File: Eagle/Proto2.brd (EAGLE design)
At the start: 100 x 80 mm, 297 parts, among them Q1 310mA/60V/1.6Ω, Q10 310mA/60V/1.6Ω, Q129 310mA/60V/1.6Ω, Q13 310mA/60V/1.6Ω, Q130 310mA/60V/1.6Ω, Q131 310mA/60V/1.6Ω, Q132 310mA/60V/1.6Ω, Q133 310mA/60V/1.6Ω, Q134 310mA/60V/1.6Ω, Q135 310mA/60V/1.6Ω, Q136 310mA/60V/1.6Ω, Q137 310mA/60V/1.6Ω, Q138 310mA/60V/1.6Ω, Q139 310mA/60V/1.6Ω, Q14 310mA/60V/1.6Ω, Q140 310mA/60V/1.6Ω, Q141 310mA/60V/1.6Ω, Q142 310mA/60V/1.6Ω, Q143 310mA/60V/1.6Ω, Q144 310mA/60V/1.6Ω, Q145 310mA/60V/1.6Ω, Q146 310mA/60V/1.6Ω, Q147 310mA/60V/1.6Ω, Q148 310mA/60V/1.6Ω, Q149 310mA/60V/1.6Ω, Q150 310mA/60V/1.6Ω, Q151 310mA/60V/1.6Ω, Q152 310mA/60V/1.6Ω, Q153 310mA/60V/1.6Ω, Q154 310mA/60V/1.6Ω, Q155 310mA/60V/1.6Ω, Q156 310mA/60V/1.6Ω, Q157 310mA/60V/1.6Ω, Q158 310mA/60V/1.6Ω, Q159 310mA/60V/1.6Ω, Q160 310mA/60V/1.6Ω, Q17 310mA/60V/1.6Ω, Q18 310mA/60V/1.6Ω, Q193 310mA/60V/1.6Ω, Q194 310mA/60V/1.6Ω, Q195 310mA/60V/1.6Ω, Q196 310mA/60V/1.6Ω, Q197 310mA/60V/1.6Ω, Q198 310mA/60V/1.6Ω, Q199 310mA/60V/1.6Ω, Q2 310mA/60V/1.6Ω, Q200 310mA/60V/1.6Ω, Q201 310mA/60V/1.6Ω, Q202 310mA/60V/1.6Ω, Q203 310mA/60V/1.6Ω, Q204 310mA/60V/1.6Ω, Q205 310mA/60V/1.6Ω, Q206 310mA/60V/1.6Ω, Q207 310mA/60V/1.6Ω, Q208 310mA/60V/1.6Ω, Q209 310mA/60V/1.6Ω, Q21 310mA/60V/1.6Ω, Q210 310mA/60V/1.6Ω, Q211 310mA/60V/1.6Ω, Q212 310mA/60V/1.6Ω, Q213 310mA/60V/1.6Ω, Q214 310mA/60V/1.6Ω, Q215 310mA/60V/1.6Ω, Q216 310mA/60V/1.6Ω, Q217 310mA/60V/1.6Ω, Q218 310mA/60V/1.6Ω, Q219 310mA/60V/1.6Ω, Q22 310mA/60V/1.6Ω, Q220 310mA/60V/1.6Ω, Q221 310mA/60V/1.6Ω, Q222 310mA/60V/1.6Ω, Q223 310mA/60V/1.6Ω, Q224 310mA/60V/1.6Ω, Q25 310mA/60V/1.6Ω, Q257 310mA/60V/1.6Ω, Q258 310mA/60V/1.6Ω, Q259 310mA/60V/1.6Ω, Q26 310mA/60V/1.6Ω, Q260 310mA/60V/1.6Ω, Q261 310mA/60V/1.6Ω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

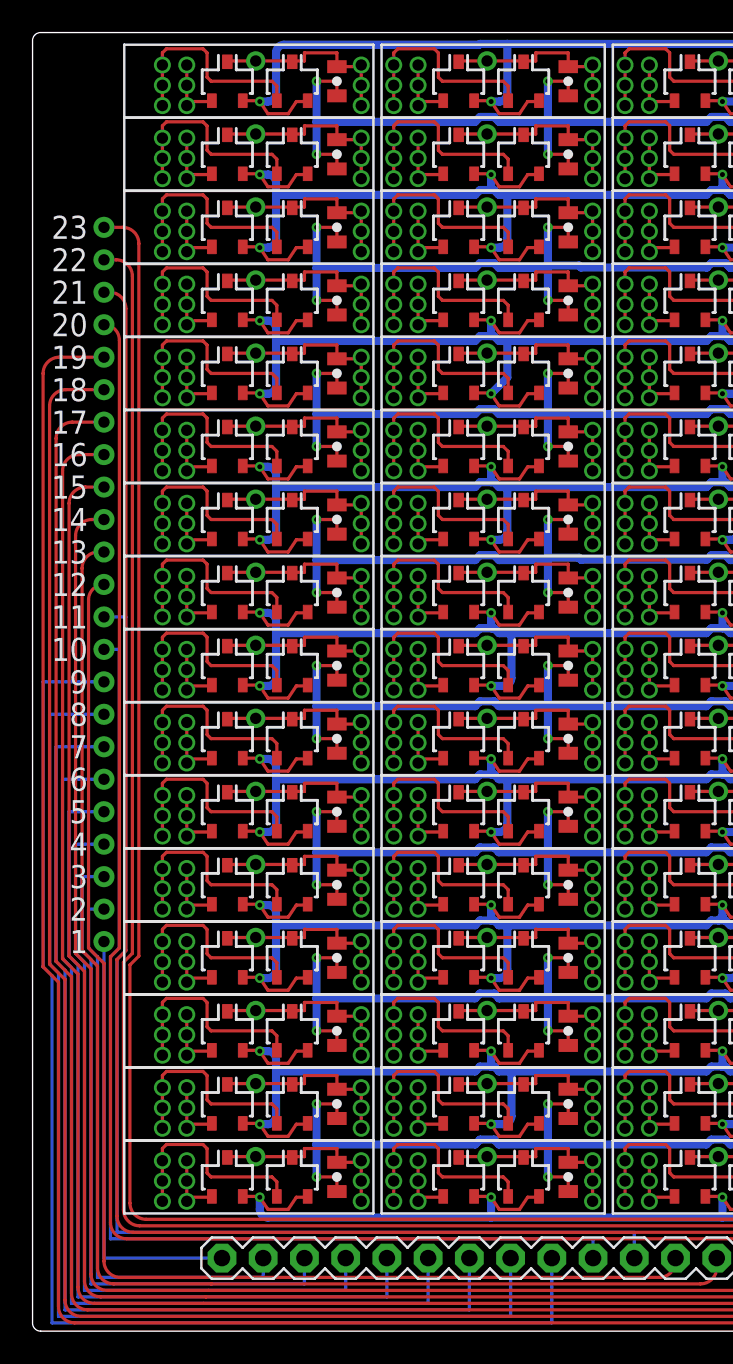
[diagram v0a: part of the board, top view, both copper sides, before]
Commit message: Silk cleanup. Routing of GND instead of floodfill
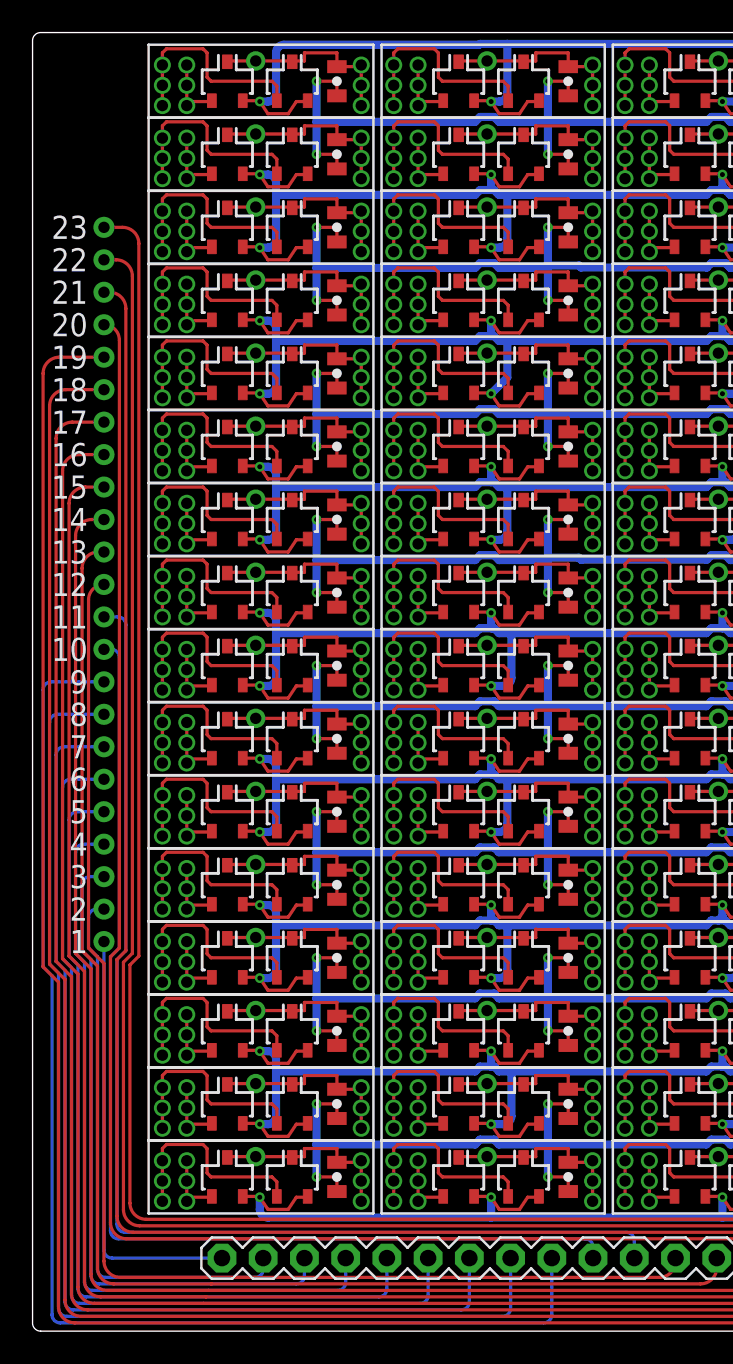
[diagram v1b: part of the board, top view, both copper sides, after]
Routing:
- net P5: track 53.7 -> 52.8 mm
- net P4: track 47.5 -> 46.7 mm
- net P9: track 78.2 -> 77.4 mm
- net P8: track 72.1 -> 71.2 mm
- net P7: track 66.0 -> 65.1 mm
- net P3: track 41.4 -> 40.5 mm
- net P2: track 35.3 -> 34.4 mm
- net P11: track 72.9 -> 72.1 mm
- net P10: track 68.4 -> 67.5 mm
- net P6: track 59.8 -> 59.0 mm
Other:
- board text added: "Dual NOR proto Rev 1"
- board text added: "SmallRoomLabs"

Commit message: Updated boards with pcb template
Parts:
- moved C10 7.00 mm to (93.8, 55.0)
- moved C12 7.00 mm to (93.8, 64.0)
- moved C14 7.00 mm to (93.8, 73.0)
- moved C16 7.00 mm to (93.8, 82.0)
- moved C4 7.00 mm to (93.8, 28.0)
- moved C6 7.00 mm to (93.8, 37.0)
- moved C8 7.00 mm to (93.8, 46.0)
- moved Q1 7.00 mm to (12.0, 16.5)
- moved Q10 7.00 mm to (16.0, 25.5)
- moved Q129 7.00 mm to (40.5, 16.5)
- moved Q13 7.00 mm to (12.0, 30.0)
- moved Q130 7.00 mm to (44.5, 16.5)
- moved Q131 7.00 mm to (40.5, 21.0)
- moved Q132 7.00 mm to (44.5, 21.0)
- moved Q133 7.00 mm to (40.5, 25.5)
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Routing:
- net GND: track 1536.7 -> 1695.6 mm
- net N$2: track 1261.0 -> 1207.5 mm
- net VCC: track 1150.1 -> 1131.3 mm
- net P17: track 109.4 -> 120.8 mm
- net P16: track 103.2 -> 114.1 mm
- net P25: track 39.4 -> 50.0 mm
- net P15: track 97.1 -> 107.4 mm
- net P14: track 91.0 -> 101.3 mm
- net P13: track 84.8 -> 94.5 mm
- net P9: track 77.4 -> 85.6 mm
- net P19: track 121.7 -> 113.5 mm
- net P8: track 71.2 -> 79.1 mm
- net P12: track 78.7 -> 86.6 mm
- net P7: track 65.1 -> 72.8 mm
- net P6: track 59.0 -> 66.4 mm
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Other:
- board size 100 x 80 mm -> 100 x 100 mm
- board text added: "NOR2 proto rev1"
- board text removed: "Dual NOR proto Rev 1"
